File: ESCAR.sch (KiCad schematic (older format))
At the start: 38 parts, among them P1 MICRO_SD, P2 BREADBOARD, P3 PROGRAM, P4 MOTOR_B, P5 MOTOR_A, P6 CONN_01X10, P7 CONN_01X10, P8 POWER_IN, SW1 RESET, SW2 MULTIFUNCTION_SW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

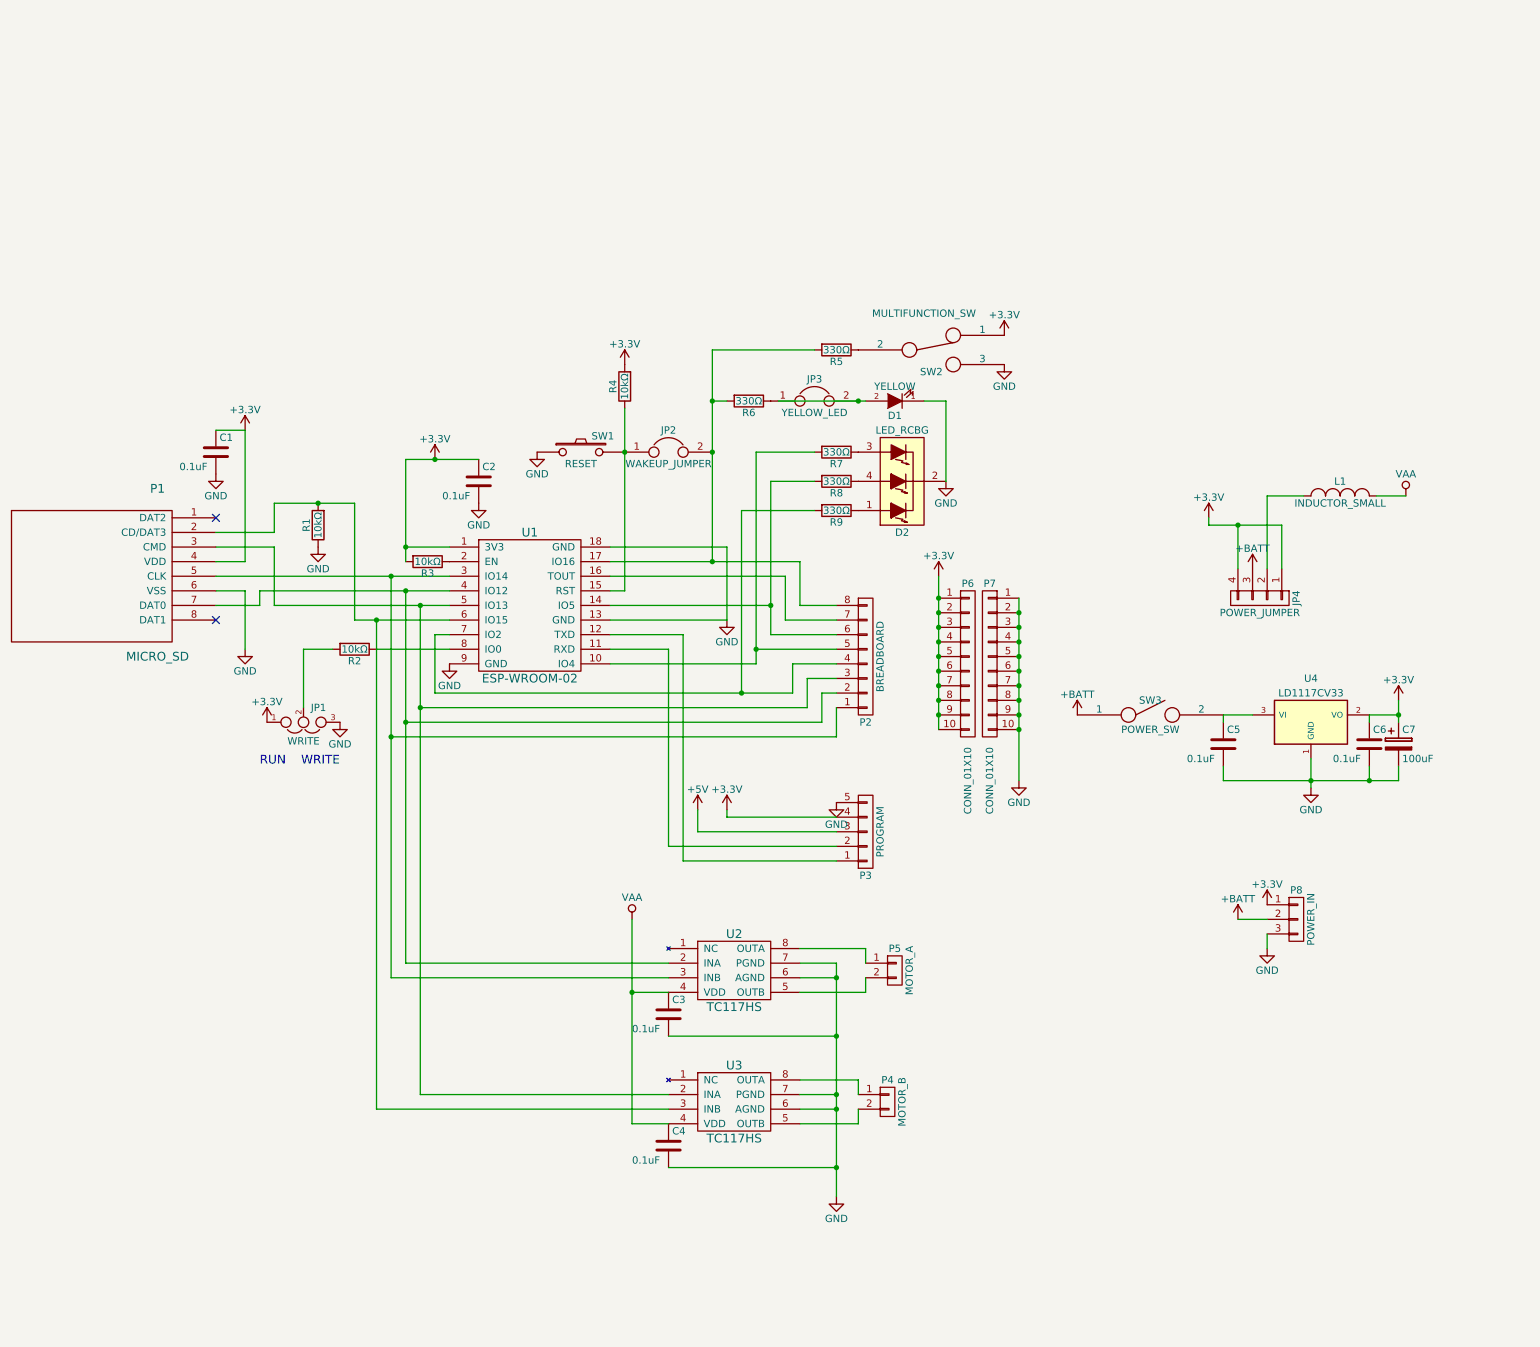
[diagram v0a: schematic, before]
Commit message: add dividing resisters for RX pin , and organized many point.
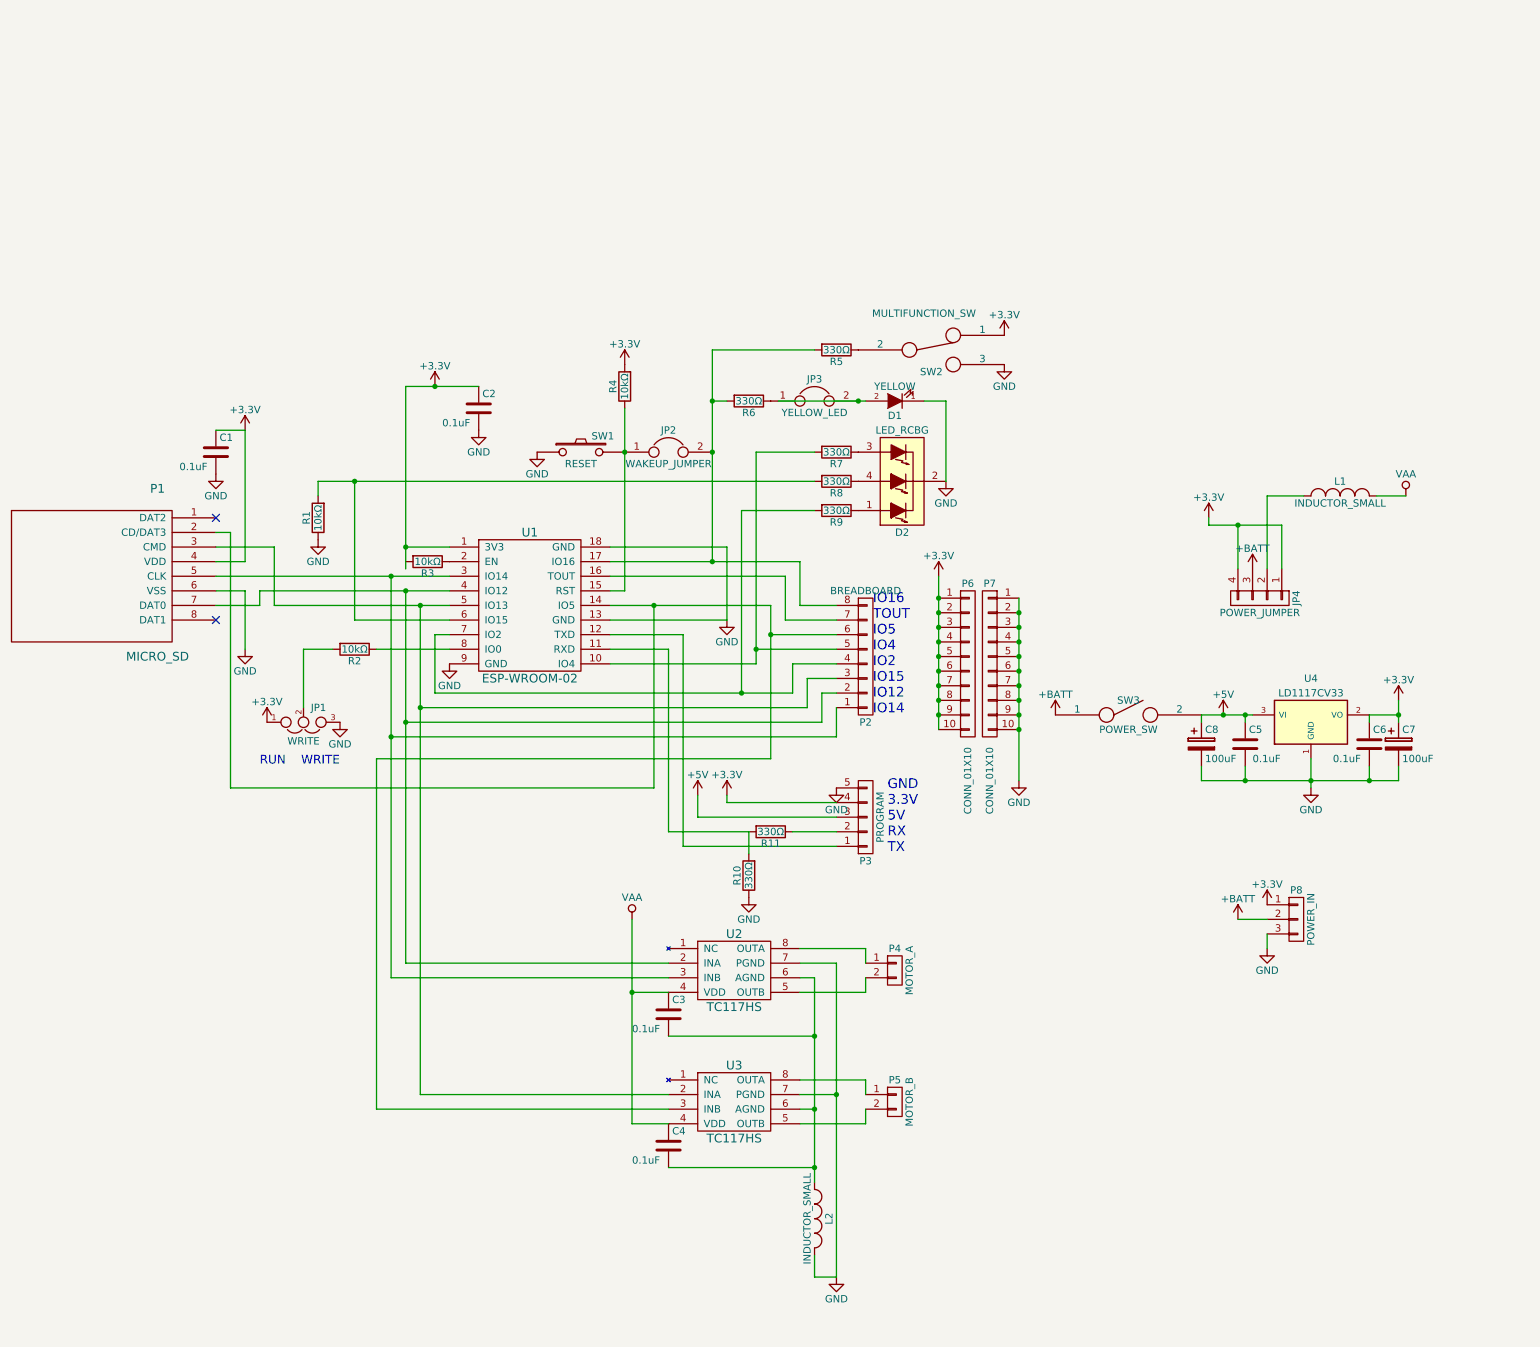
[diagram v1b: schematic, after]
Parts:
- added C8: 100uF, Capacitors_ThroughHole:C_Radial_D6.3_L11.2_P2.5, symbol CP
- added L2: INDUCTOR_SMALL, Inductors:Inductor_1212, symbol INDUCTOR_SMALL
- added R10, R11: 330Ω, Resistors_SMD:R_1206_HandSoldering, symbol R
- P4: value MOTOR_B -> MOTOR_A
- P5: value MOTOR_A -> MOTOR_B
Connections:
- net +3V3: no longer R3.2
- net +5V: now also C5.1, SW3.2, U4.3 (VI), C8.1
- net GND: now also C8.2, L2.2, R10.1; no longer C3.2, C4.2, U2.6 (AGND), U3.6 (AGND)
- net at P1.2 (CD/DAT3), U3.3 (INB): now also P2.6 (P6), U1.14 (IO5); no longer R1.2, U1.6 (IO15)
- net at U1.11 (RXD): now also R10.2, R11.2; no longer P3.2 (P2)
- net at U2.5 (OUTB): now also P4.2 (P2); no longer P5.2 (P2)
- net at U2.8 (OUTA): now also P4.1 (P1); no longer P5.1 (P1)
- net at U3.5 (OUTB): now also P5.2 (P2); no longer P4.2 (P2)
- net at U3.8 (OUTA): now also P5.1 (P1); no longer P4.1 (P1)
- new net: R1.2, R8.2, U1.6 (IO15)
- new net: P3.2 (P2), R11.1
- new net: C3.2, C4.2, L2.1, U2.6 (AGND), U3.6 (AGND)
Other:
- note added: "GND\n3.3V\n5V\nRX\nTX"
- note added: "IO16\nTOUT\nIO5\nIO4\nIO2\nIO15\nIO12\nIO14"
- moved on the sheet: C2, C5, P3, P4, P5, R1, SW3

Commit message: Ver20160517 Release. Add USB switch function, change GPIO assign.
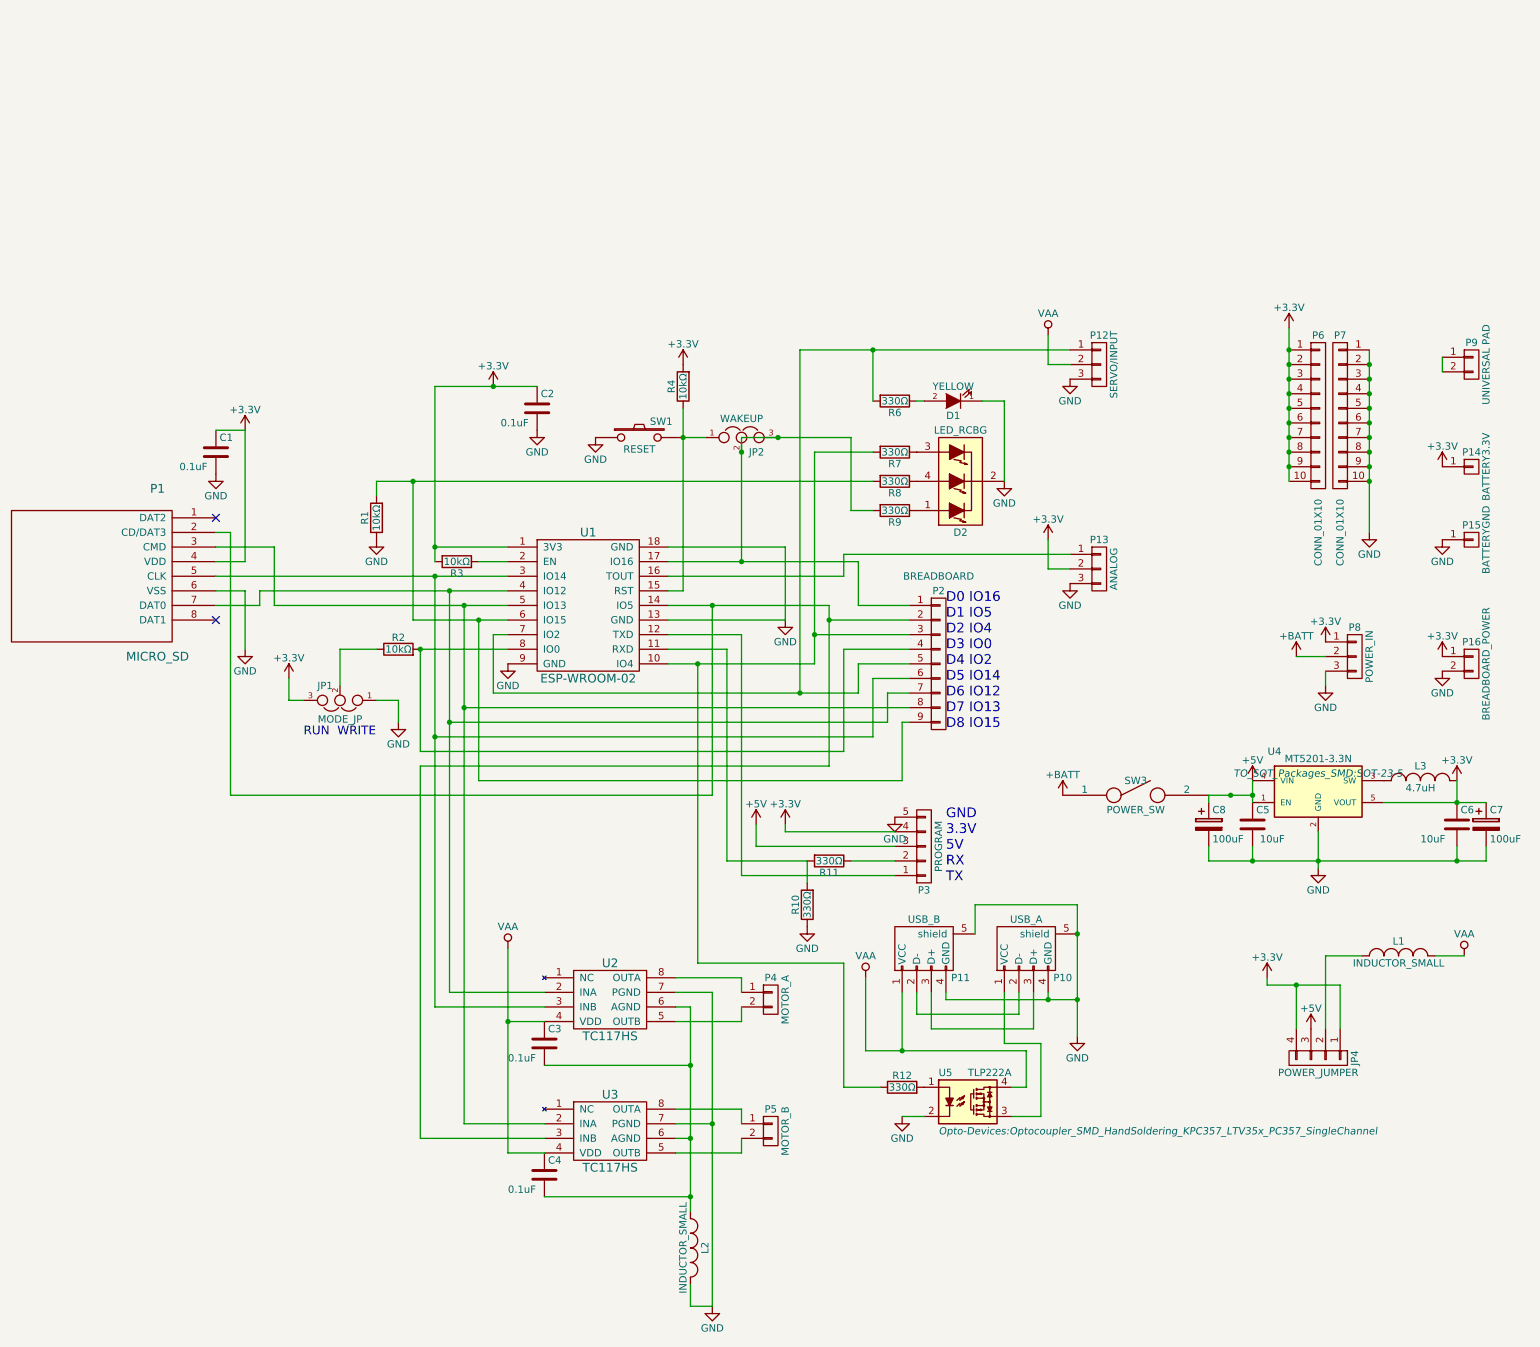
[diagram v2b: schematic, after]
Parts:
- removed JP2: WAKEUP_JUMPER, library:Soldar_Jumper_Unconnected, symbol JUMPER
- removed JP3: YELLOW_LED, library:Soldar_Jumper_Unconnected, symbol JUMPER
- removed P2: BREADBOARD, Pin_Headers:Pin_Header_Straight_1x08, symbol CONN_01X08
- removed R5: 330Ω, Resistors_SMD:R_1206_HandSoldering, symbol R
- removed SW2: MULTIFUNCTION_SW, Buttons_Switches_ThroughHole:SW_Micro_SPST, symbol SWITCH_INV
- removed U4: LD1117CV33, TO_SOT_Packages_THT:TO-220_Neutral123_Vertical, symbol NCP1117ST33T3G
- added JP2: WAKEUP, library:Solder_Jumper_3, symbol JUMPER3
- added L3: 4.7uH, library:C_1206_HandSoldering_Small, symbol INDUCTOR_SMALL
- added P10: USB_A, library:USB_A_Vertical_Short, symbol USB_A
- added P11: USB_B, Pin_Headers:Pin_Header_Straight_1x05, symbol USB_B
- added P12: SERVO/INPUT, Pin_Headers:Pin_Header_Straight_1x03, symbol CONN_01X03
- added P13: ANALOG, Pin_Headers:Pin_Header_Straight_1x03, symbol CONN_01X03
- added P14: BATTERY3.3V, Wire_Pads:SolderWirePad_single_0-8mmDrill, symbol CONN_01X01
- added P15: BATTERYGND, Wire_Pads:SolderWirePad_single_0-8mmDrill, symbol CONN_01X01
- added P16: BREADBOARD_POWER, library:Padmatrix-wide-02x01, symbol CONN_01X02
- added P2: BREADBOARD, library:SolderWirePad_Oval_9xInline_0-6mmDrill, symbol CONN_01X09
- added P9: UNIVERSAL PAD, library:Padmatrix-wide-02x01, symbol CONN_01X02
- added R12: 330Ω, library:R_1206_HandSoldering_Small, symbol R
- added U4: MT5201-3.3N, TO_SOT_Packages_SMD:SOT-23-5, symbol MT5201-3.3N
- added U5: TLP222A, Opto-Devices:Optocoupler_SMD_HandSoldering_KPC357_LTV35x_PC357_SingleChannel, symbol TLP222A
- C1, C2, C3, C4: footprint Capacitors_SMD:C_1206_HandSoldering -> library:C_1206_HandSoldering_Small
- C5, C6: value 0.1uF -> 10uF; footprint Capacitors_SMD:C_1206_HandSoldering -> library:C_1206_HandSoldering_Small
- JP1: value WRITE -> MODE_JP
- L1, L2: footprint Inductors:Inductor_1212 -> library:C_1206_HandSoldering_Small
- R1, R10, R11, R2, R3, R4, R6, R7, R8, R9: footprint Resistors_SMD:R_1206_HandSoldering -> library:R_1206_HandSoldering_Small
- SW1: footprint Buttons_Switches_ThroughHole:SW_DIP_x1_Slide -> library:SW_SMD_3x6_WithHole
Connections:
- net +3V3: now also JP1.3, R3.2, L3.2, P13.2 (P2), P14.1 (P1), P16.1 (P1), U4.5 (VOUT); no longer JP1.1
- net +5V: now also JP4.3 (P3), U4.1 (EN), U4.4 (VIN)
- net +BATT: no longer JP4.3 (P3)
- net GND: now also JP1.1, P10.4 (GND), P10.5 (shield), P11.4 (GND), P11.5 (shield), P12.3 (P3), P13.3 (P3), P15.1 (P1), P16.2 (P2), U4.2 (GND), U5.2; no longer JP1.3
- net VAA: now also P11.1 (VCC), P12.2 (P2), U5.4
- net at P1.2 (CD/DAT3), U1.14 (IO5), U3.3 (INB): now also P2.2 (P2)
- net at P1.3 (CMD), U1.5 (IO13), U3.2 (INA): now also P2.8 (P8)
- net at P1.5 (CLK), U1.3 (IO14), U2.3 (INB): now also P2.6 (P6)
- net at P1.7 (DAT0), U1.4 (IO12), U2.2 (INA): now also P2.7 (P7)
- net at R9.2: now also U1.17 (IO16), JP2.2, JP2.3, P2.1 (P1); no longer U1.7 (IO2)
- net at R7.2, U1.10 (IO4): now also P2.3 (P3), R12.1
- net at U1.16 (TOUT): now also P13.1 (P1)
- net at R6.2: now also U1.7 (IO2), P12.1 (P1), P2.5 (P5); no longer U1.17 (IO16)
- net at R1.2, R8.2, U1.6 (IO15): now also P2.9 (P9)
- net at R4.1, SW1.2, U1.15 (RST): now also JP2.1
- net at U1.8 (IO0): now also R2.2, P2.4 (P4); no longer R2.1
- net at JP1.2: now also R2.1; no longer R2.2
- net at R6.1: now also D1.2 (A)
- new net: P10.1 (VCC), U5.3
- new net: P10.2 (D-), P11.2 (D-)
- new net: P10.3 (D+), P11.3 (D+)
- new net: R12.2, U5.1
- new net: P9.1 (P1), P9.2 (P2)
- new net: L3.1, U4.3 (SW)
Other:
- note added: "D0 IO16\nD1 IO5\nD2 IO4\nD3 IO0\nD4 IO2\nD5 IO14\nD6 IO12\nD7 IO13\nD8 IO15"
- note removed: "IO16\nTOUT\nIO5\nIO4\nIO2\nIO15\nIO12\nIO14"
- moved on the sheet: C2, C3, C4, C5, C6, C7, C8, D1, D2, JP4, L1, L2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

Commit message: Ver20160617 Release. change PORT mapping, pin header hole size, silk. and few bug fix
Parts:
- added C9: 0.1uF, library:C_1206_HandSoldering_Small, symbol C
- added JP3: JUMPER, library:Solder_Jumper_2, symbol JUMPER
- added R13, R5: 4.7kΩ, library:R_1206_HandSoldering_Small, symbol R
- JP1, P12, P13, P8: footprint Pin_Headers:Pin_Header_Straight_1x03 -> library:SolderWirePad_Oval_3xInline_0-65mmDrill
- JP4: footprint Pin_Headers:Pin_Header_Straight_1x04 -> library:SolderWirePad_Oval_4xInline_0-65mmDrill
- P3: footprint Pin_Headers:Pin_Header_Straight_1x05 -> library:SolderWirePad_Oval_5xInline_0-65mmDrill
- P4, P5: footprint Pin_Headers:Pin_Header_Straight_1x02 -> library:SolderWirePad_Oval_2xInline_0-65mmDrill
- R1, R2, R3, R4: value 10kΩ -> 4.7kΩ
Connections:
- net +3V3: now also R5.2
- net GND: now also C9.2, R13.1
- net at P1.2 (CD/DAT3), U3.3 (INB): now also JP2.2, JP2.3, P2.1 (P1), R9.2, U1.17 (IO16); no longer P2.2 (P2), U1.14 (IO5)
- net at R3.1, U1.2 (EN): now also C9.1
- net at R10.2, R11.2, U1.11 (RXD): now also P3.2 (P2), R11.1, JP3.1, JP3.2
- net at P13.1 (P1), U1.16 (TOUT): now also R13.2
- net at P2.5 (P5), R6.2, U1.7 (IO2): now also R5.1; no longer P12.1 (P1)
- new net: P12.1 (P1), P2.2 (P2), U1.14 (IO5)
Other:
- moved on the sheet: C2, R10, R3
